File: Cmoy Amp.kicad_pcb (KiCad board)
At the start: 2 copper layers, 67.2 x 39.5 mm, 23 parts, among them U1 OPA2132PA-ND

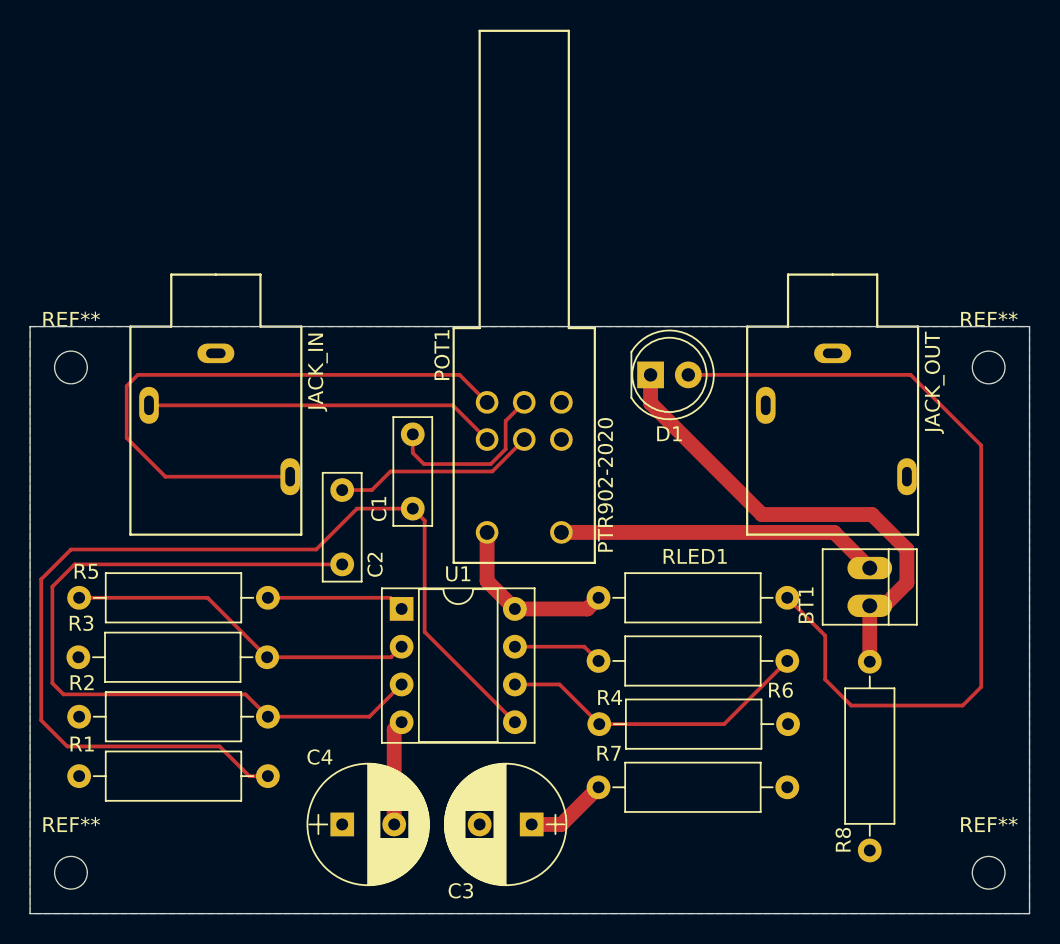
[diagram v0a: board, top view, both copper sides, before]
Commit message: Reduce PCB size
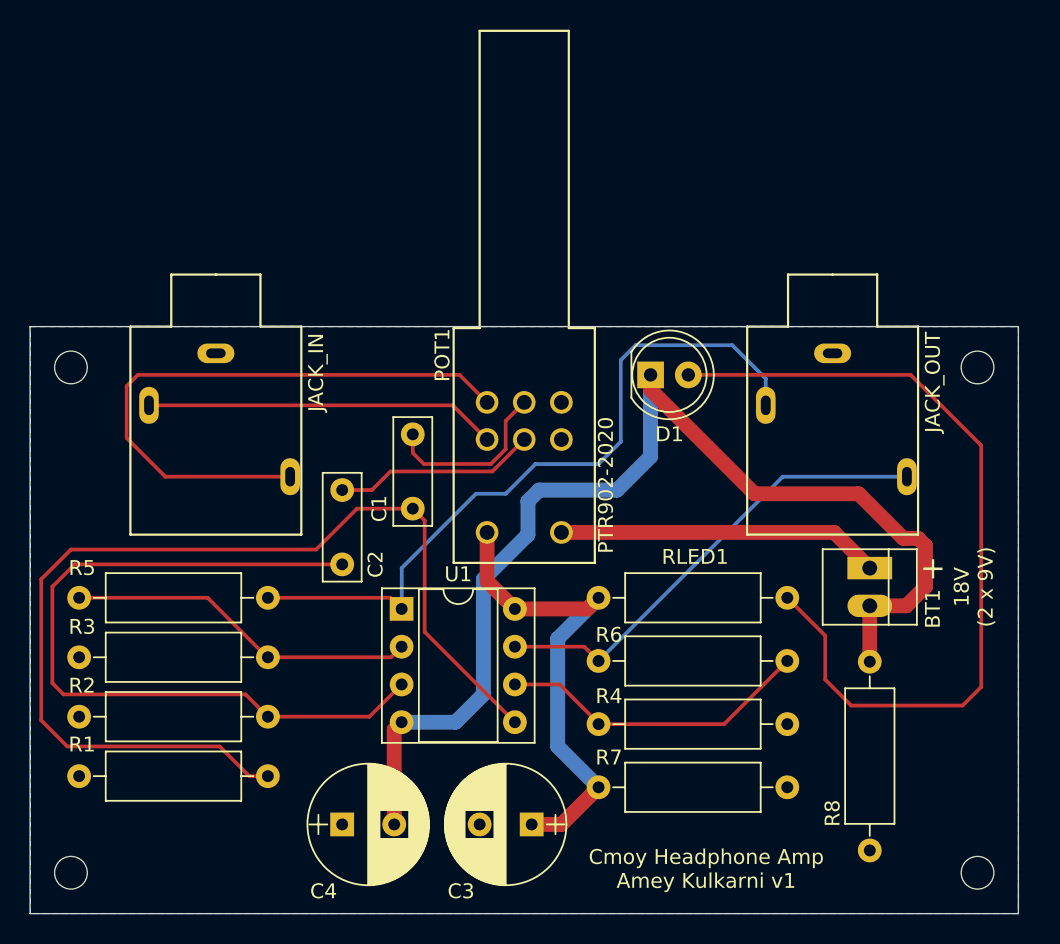
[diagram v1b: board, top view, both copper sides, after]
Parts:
- removed the REF** at (181.2, 136.8)
- removed the REF** at (181.2, 102.8)
- added REF**: MountingHole_2.2mm_M2, Mounting_Holes:MountingHole_2.2mm_M2, F.Cu at (180.5, 136.8)
- added REF**: MountingHole_2.2mm_M2, Mounting_Holes:MountingHole_2.2mm_M2, F.Cu at (180.5, 102.8)
- moved R4 0.05 mm to (167.7, 126.8)
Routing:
- net /OutB: track 9.31 -> 48.7 mm
- net V-: track 39.5 -> 77.2 mm
- net /OutA: track 6.03 -> 31.9 mm
- net V+: track 17.4 -> 32.4 mm
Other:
- board size 67.2 x 39.5 mm -> 66.5 x 39.5 mm
- board text added: "+"
- board text added: "18V (2 x 9V)"
- board text added: "Cmoy Headphone Amp Amey Kulkarni v1"

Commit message: Update PCB layout
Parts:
- removed JACK_IN, JACK_OUT: SJ1-3513, MyLib:SJ1-3513
- removed the REF** at (180.5, 136.8)
- removed the REF** at (119.5, 136.8)
- removed the REF** at (180.5, 102.8)
- removed the REF** at (119.5, 102.8)
- added JACK_IN1: SJ1-3513, MyLib:SJ1-3513, F.Cu at (129.2, 105.2)
- added JACK_OUT1: SJ1-3513, MyLib:SJ1-3513, F.Cu at (170.8, 105.2)
- added REF**: MountingHole_2.2mm_M2, Mounting_Holes:MountingHole_2.2mm_M2, F.Cu at (119.8, 102.8)
- added REF**: MountingHole_2.2mm_M2, Mounting_Holes:MountingHole_2.2mm_M2, F.Cu at (119.8, 136.8)
- added REF**: MountingHole_2.2mm_M2, Mounting_Holes:MountingHole_2.2mm_M2, F.Cu at (180.2, 136.8)
- added REF**: MountingHole_2.2mm_M2, Mounting_Holes:MountingHole_2.2mm_M2, F.Cu at (180.2, 102.8)
- moved R1 13.0 mm to (133.2, 117.2)
- moved RLED1 12.8 mm to (167.8, 118.2), turned to 180 degrees
- moved C3 12.5 mm to (138.0, 133.0), turned to 0 degrees
- moved C4 9.26 mm to (147.0, 133.0)
- moved R2 3.04 mm to (133.2, 129.2)
- moved R3 3.04 mm to (120.5, 125.2)
- moved R5 3.04 mm to (133.2, 121.2)
- moved D1 2.75 mm to (161.2, 103.2), turned to 180 degrees
- moved R4 0.05 mm to (167.8, 126.8)
- moved R6 0.05 mm to (155.1, 122.5)
- moved R7 0.05 mm to (155.1, 131.0)
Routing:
- net V-: track 77.2 -> 0.00 mm
- net Net-(C1-Pad1): track 70.5 -> 29.4 mm
- net V+: track 32.4 -> 69.9 mm
- net Net-(D1-Pad2): track 56.2 -> 24.2 mm
- net /OutB: track 48.7 -> 42.5 mm
- net Net-(C2-Pad1): track 52.0 -> 54.0 mm
- net Net-(R3-Pad2): track 23.7 -> 24.4 mm
- added copper zone on F.Cu, net V-

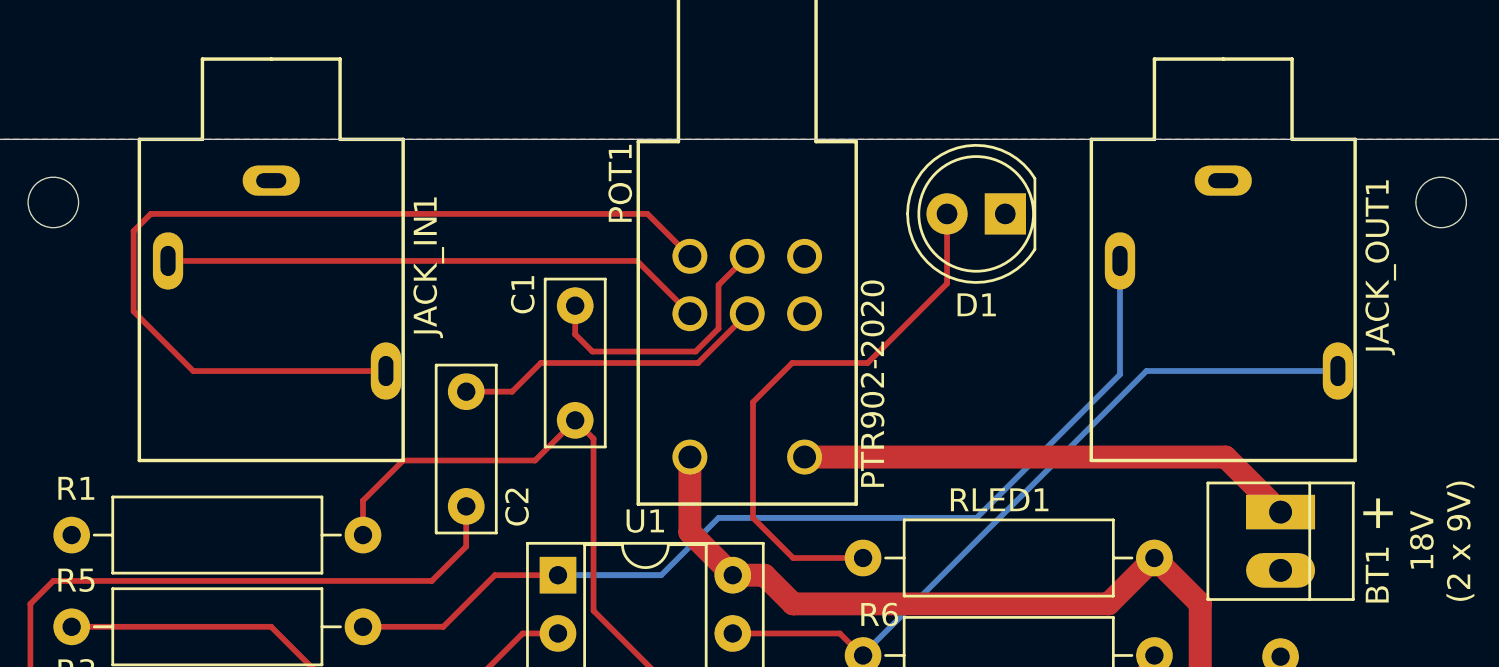
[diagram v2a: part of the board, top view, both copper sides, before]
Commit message: Add 3D models
Added 3D models for the audio jack and the potentiometer-switch
footprints
Fixed 3D models for all other components so that the 3D view shows
all the models
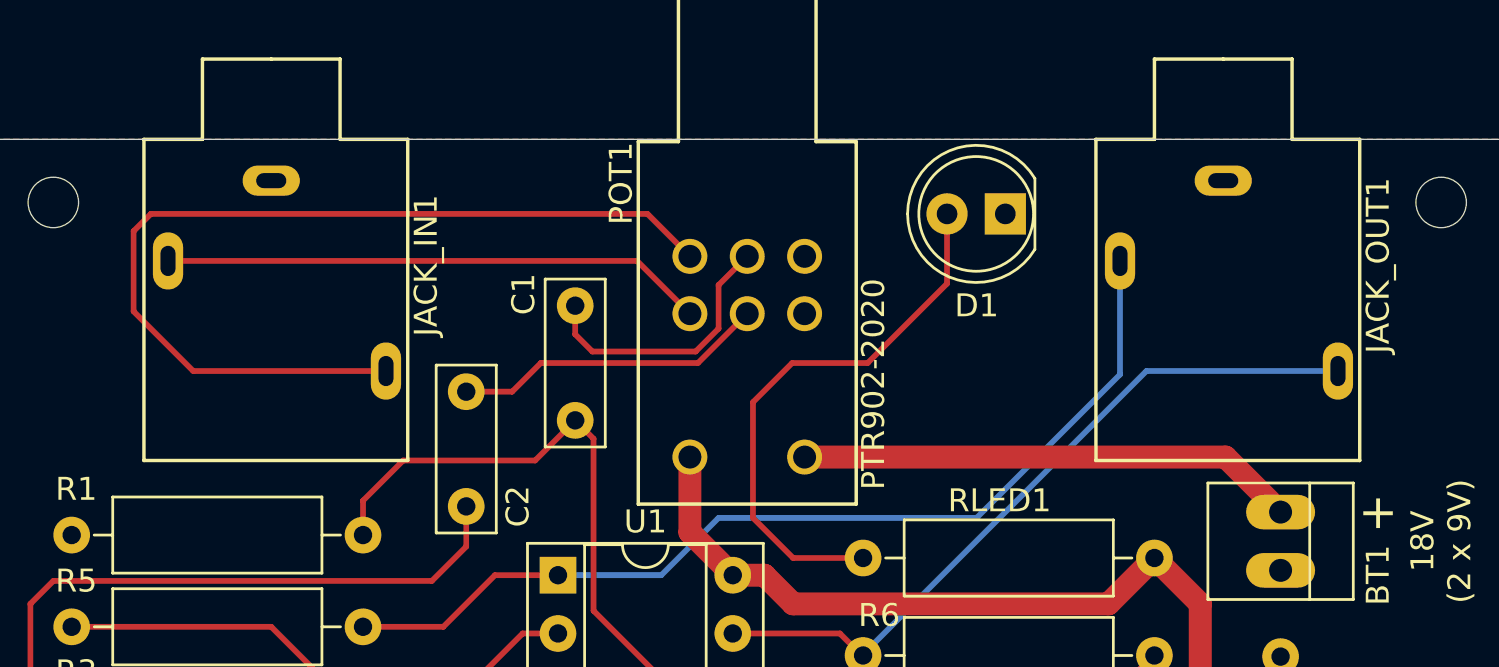
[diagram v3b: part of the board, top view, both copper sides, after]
